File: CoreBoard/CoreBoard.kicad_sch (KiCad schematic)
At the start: 71 parts, among them J1 RJ45_LED_Shielded, SW1 SW_Push, SW10 SW_Push, SW12 SW_DIP_x07, SW2 SW_Push, SW3 SW_Push, SW4 SW_Push, SW5 SW_Push, SW6 SW_Push, SW7 SW_Push, SW8 SW_Push, SW9 SW_Push, U1 OKI, U2 Teensy4.1_DEV-16771, U3 SHHD003A0A, U4 GY-521, U5 ATA6561, U6 74HC148, U7 74HC148, U8 74HC00

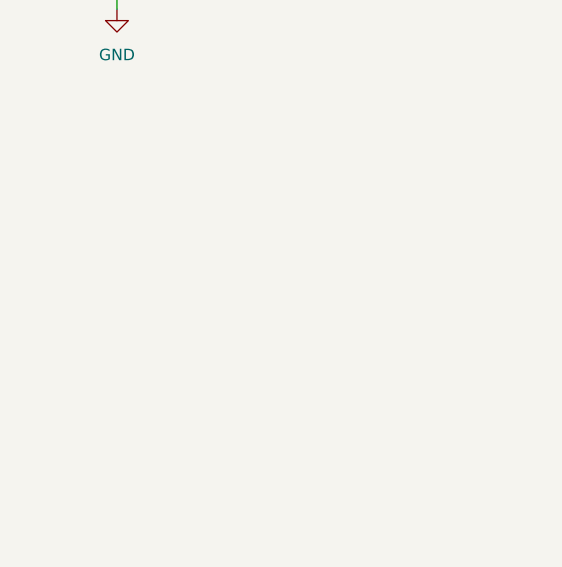
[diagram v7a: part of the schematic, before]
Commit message: Added mounting holes
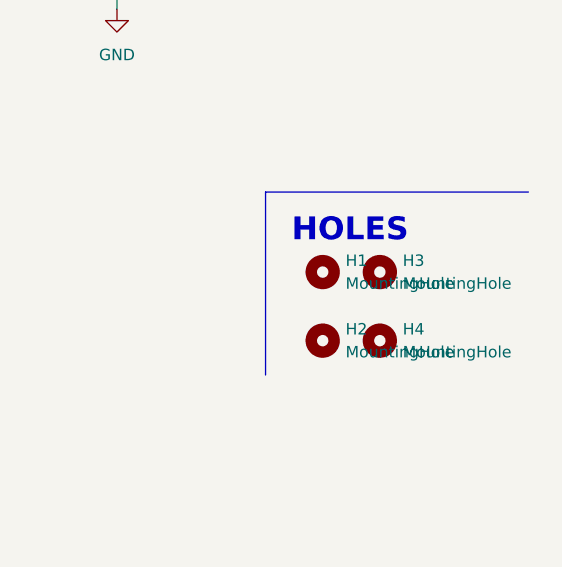
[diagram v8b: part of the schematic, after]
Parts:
- added H1, H2, H3, H4: MountingHole, symbol Mechanical:MountingHole
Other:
- note added: "HOLES"
